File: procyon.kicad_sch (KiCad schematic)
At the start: 26 parts, among them J1 Conn_01x07_Pin, Q1 AO3401A, U1 mXT336UD-MAU002

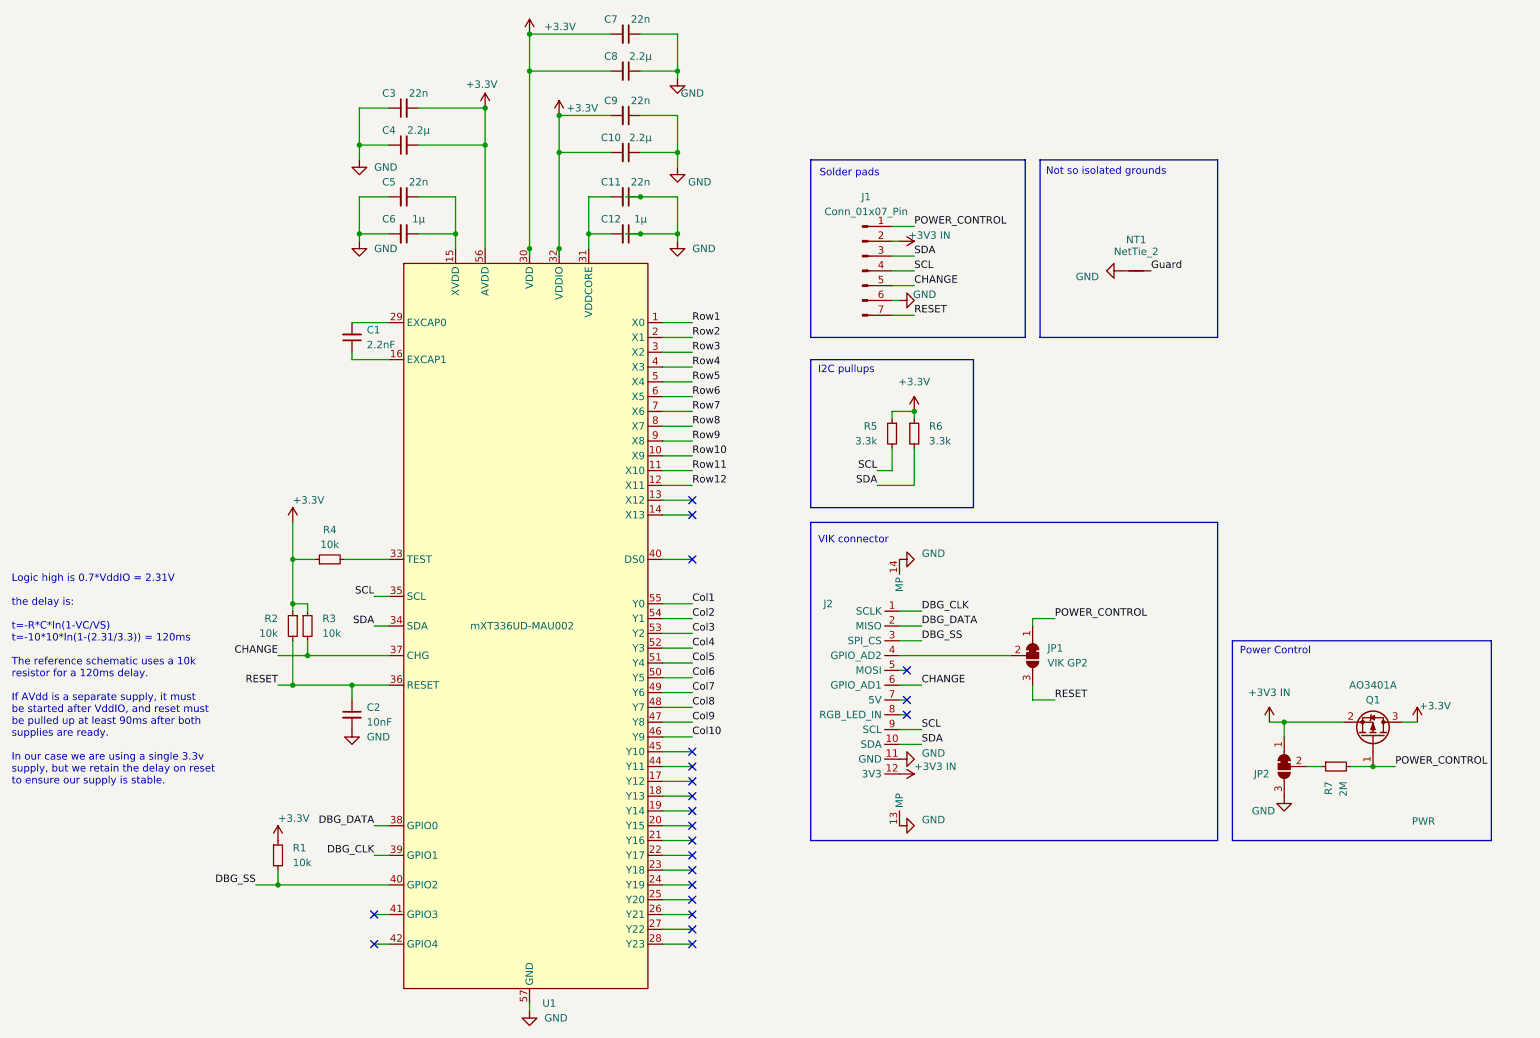
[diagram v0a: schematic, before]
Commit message: Swap from a 12x10 to a 10x12 matrix so we can use self capacitance measurements.
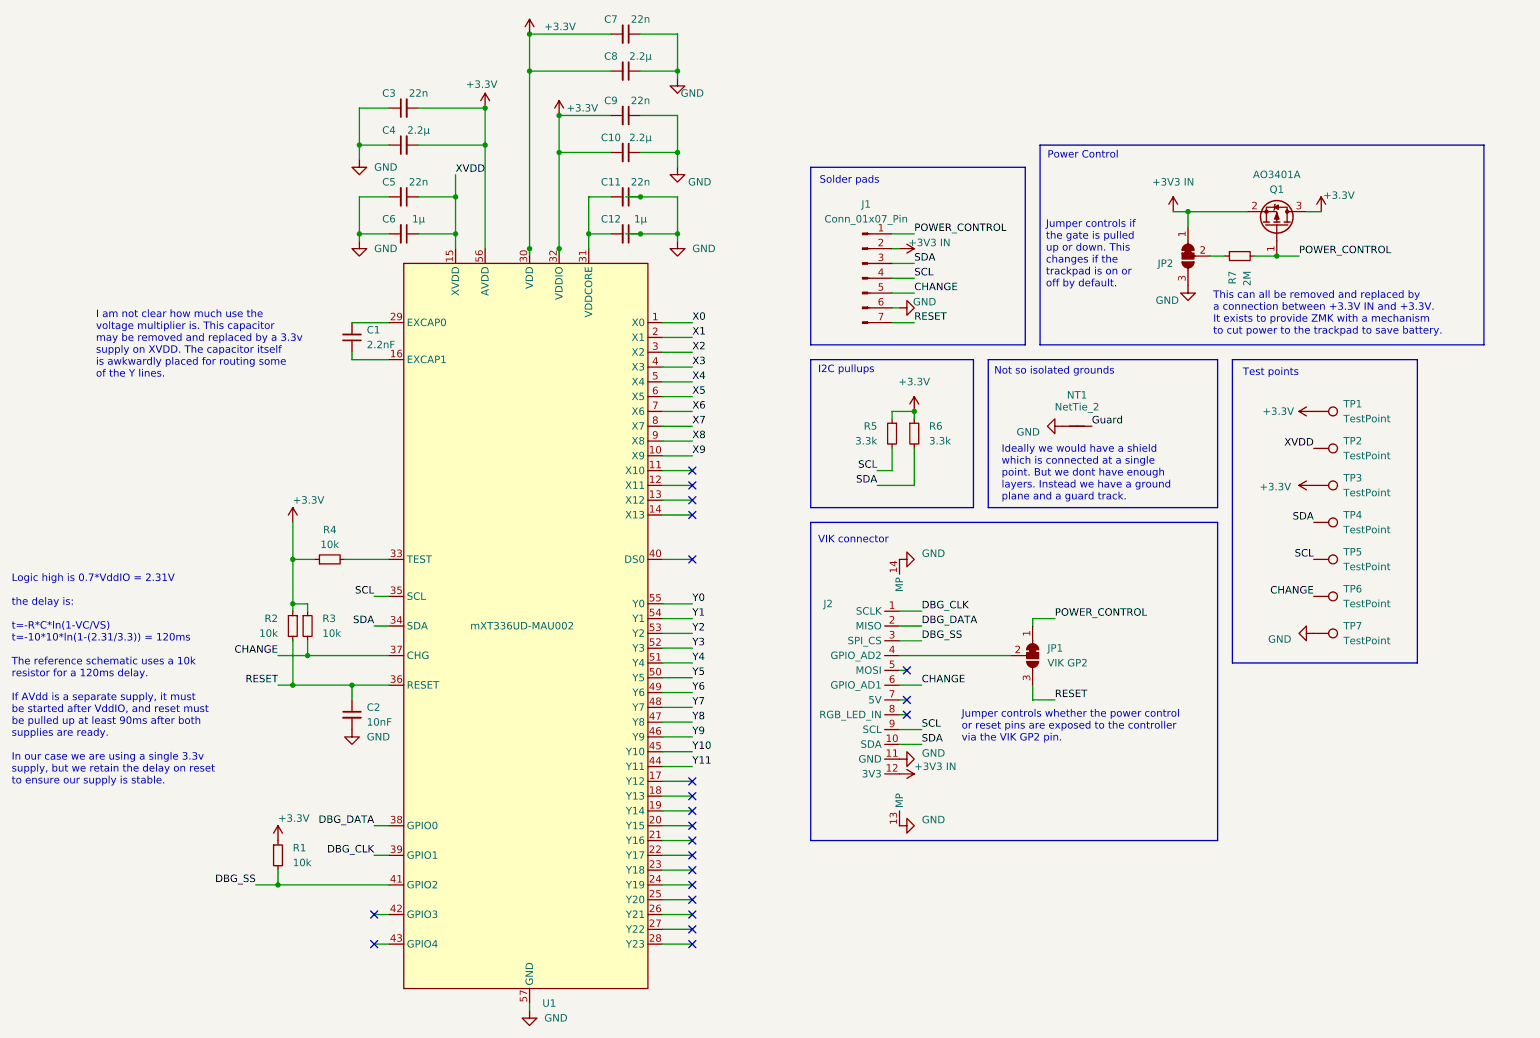
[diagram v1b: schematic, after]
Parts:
- added TP1, TP2, TP3, TP4, TP5, TP6, TP7: TestPoint, TestPoint:TestPoint_Pad_D1.0mm, symbol Connector:TestPoint
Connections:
- net +3.3V: now also TP1.1, TP3.1
- net CHANGE: now also TP6.1
- net DBG_SS: now also U1.41 (GPIO2); no longer U1.40 (GPIO2)
- net GND: now also TP7.1
- net SCL: now also TP5.1
- net SDA: now also TP4.1
- net XVDD: now reaches C5.1, C6.1, U1.15 (XVDD)
- net XVDD: now also TP2.1
- net Y11: now reaches U1.44 (Y11)
- net Y10: now reaches U1.45 (Y10)
- net Col1 renamed Y0
- net Col10 renamed Y9
- net Col2 renamed Y1
- net Col3 renamed Y2
- net Col4 renamed Y3
- net Col5 renamed Y4
- net Col6 renamed Y5
- net Col7 renamed Y6
- net Col8 renamed Y7
- net Col9 renamed Y8
- net Row1 renamed X0
- net Row10 renamed X9
- net Row11: no longer names the net of U1.11 (X10)
- net Row12: no longer names the net of U1.12 (X11)
- net Row2 renamed X1
- net Row3 renamed X2
- net Row4 renamed X3
- net Row5 renamed X4
- net Row6 renamed X5
- net Row7 renamed X6
- net Row8 renamed X7
- net Row9 renamed X8
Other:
- note added: "I am not clear how much use the voltage multiplier is. This capacitor may be removed and replaced by a 3.3v supply on XVDD. The capacitor itself is awkwardly placed for routing some of the Y lines."
- note added: "Ideally we would have a shield which is connected at a single point. But we dont have enough layers. Instead we have a ground plane and a guard track."
- note added: "Jumper controls if the gate is pulled up or down. This changes if the trackpad is on or off by default."
- note added: "Jumper controls whether the power control or reset pins are exposed to the controller via the VIK GP2 pin."
- note added: "Test points"
- note added: "This can all be removed and replaced by a connection between +3.3V IN and +3.3V. It exists to provide ZMK with a mechanism to cut power to the trackpad to save battery."
- moved on the sheet: J1, JP2, NT1, Q1, R7

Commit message: Add TP8.
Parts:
- added TP8: TestPoint, TestPoint:TestPoint_Pad_D1.0mm, symbol Connector:TestPoint
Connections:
- net +3V3 IN: now also TP8.1
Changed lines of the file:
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@@
 	(rectangle
 		(start 228.6 80.01)
-		(end 260.35 132.08)
+		(end 260.35 144.78)
 		(stroke
 			(width 0)
@@
 	)
 	(symbol
+		(lib_id "Connector:TestPoint")
+		(at 242.57 133.35 270)
+		(unit 1)
+		(exclude_from_sim no)
+		(in_bom yes)
+		(on_board yes)
+		(dnp no)
+		(property "Reference" "TP8"
+			(at 247.65 132.0799 90)
+			(effects
+				(font
+					(size 1.27 1.27)
+				)
+				(justify left)
+			)
+		)
+		(property "Value" "TestPoint"
+			(at 247.65 134.6199 90)
+			(effects
+				(font
+					(size 1.27 1.27)
+				)
+				(justify left)
+			)
+		)
+		(property "Footprint" "TestPoint:TestPoint_Pad_D1.0mm"
+			(at 242.57 138.43 0)
+			(effects
+				(font
+					(size 1.27 1.27)
+				)
+				(hide yes)
+			)
+		)
+		(property "Datasheet" "~"
+			(at 242.57 138.43 0)
+			(effects
+				(font
+					(size 1.27 1.27)
+				)
+				(hide yes)
+			)
+		)
+		(property "Description" "test point"
+			(at 242.57 133.35 0)
+			(effects
+				(font
+					(size 1.27 1.27)
+				)
+				(hide yes)
+			)
+		)
+		(pin "1"
+		)
+		(instances
+			(project "procyon"
+				(path "/22e83c18-ea75-4c5e-9dba-5c9f658130b9"
+					(reference "TP8")
+					(unit 1)
+				)
+			)
+		)
+	)
+	(symbol
 		(lib_id "Device:C_Small")
 		(at 77.47 76.2 180)
@@
 					(unit 1)
 				)
+			)
+		)
+	)
+	(symbol
+		(lib_id "power:+3V3")
+		(at 242.57 133.35 90)
+		(mirror x)
+		(unit 1)
+		(exclude_from_sim no)
+		(in_bom yes)
+		(on_board yes)
+		(dnp no)
+		(property "Reference" "#PWR027"
+			(at 246.38 133.35 0)
+			(effects
+				(font
+					(size 1.27 1.27)
+				)
+				(hide yes)
+			)
+		)
+		(property "Value" "+3V3 IN"
+			(at 239.268 133.35 90)
+			(effects
+				(font
+					(size 1.27 1.27)
+				)
+				(justify left)
+			)
+		)
+		(property "Footprint" ""
+			(at 242.57 133.35 0)
+			(effects
+				(font
+					(size 1.27 1.27)
+				)
+				(hide yes)
+			)
+		)
+		(property "Datasheet" ""
+			(at 242.57 133.35 0)
+			(effects
+				(font
+					(size 1.27 1.27)
+				)
+				(hide yes)
+			)
+		)
+		(property "Description" "Power symbol creates a global label with name \"+3V3\""
+			(at 242.57 133.35 0)
+			(effects
+				(font
+					(size 1.27 1.27)
+				)
+				(hide yes)
+			)
+		)
+		(pin "1"
+		)
+		(instances
+			(project "procyon"
+				(path "/22e83c18-ea75-4c5e-9dba-5c9f658130b9"
+					(reference "#PWR027")
+					(unit 1)
+				)

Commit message: Flip the power control jumper.
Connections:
- net +3V3 IN: now also JP2.3 (B); no longer JP2.1 (A)
- net GND: now also JP2.1 (A); no longer JP2.3 (B)
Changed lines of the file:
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@@
 		(lib_id "Jumper:SolderJumper_3_Bridged12")
 		(at 220.98 62.23 90)
-		(mirror x)
 		(unit 1)
 		(exclude_from_sim yes)
@@
 		(dnp no)
 		(property "Reference" "JP2"
-			(at 218.44 63.5001 90)
+			(at 218.44 60.9599 90)
 			(effects
 				(font
@@
 		)
 		(property "Value" "PWR"
-			(at 246.888 71.628 90)
+			(at 246.888 52.832 90)
 			(effects
 				(font
